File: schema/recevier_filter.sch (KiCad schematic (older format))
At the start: 14 parts, among them U7 LM358, U8 LM393

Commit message: Reception: schmidt trigger
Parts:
- removed R19: 100kΩ, symbol R
- removed R20: 10kΩ, symbol R
- added R? (x2): 4.7kΩ, symbol R
- added R?: 10kΩ, symbol R
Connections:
- net +5V: now also R?.1
- net GND: now also R?.2
- net SIGNAL: now also R?.1
- net at R18.1, U?.1: now also U8.2 (_); no longer U8.3 (+)
- new net: R?.1, R?.2, R?.2, U8.3 (+)
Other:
- note added: "Schmidt trigger"
- note removed: "Comparator"
- moved on the sheet: C?, R21, U8A
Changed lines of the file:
@@
 Comment4 ""
 $EndDescr
-Text HLabel 9700 3650 2    60   Output ~ 0
+Text HLabel 9700 3450 2    60   Output ~ 0
 SIGNAL
 $Comp
@@
 L LM393 U8
 U 1 1 5924C9D9
-P 8400 3650
-F 0 "U8" H 8550 3800 50  0000 C CNN
-F 1 "LM393" H 8650 3500 50  0000 C CNN
-F 2 "" H 8400 3650 50  0000 C CNN
-F 3 "" H 8400 3650 50  0000 C CNN
-	1    8400 3650
-	1    0    0    -1
-$EndComp
-$Comp
-L R R19
-U 1 1 5924CC18
-P 7600 3750
-F 0 "R19" V 7680 3750 50  0000 C CNN
-F 1 "100kΩ" V 7500 3750 50  0000 C CNN
-F 2 "" V 7530 3750 50  0000 C CNN
-F 3 "" H 7600 3750 50  0000 C CNN
-	1    7600 3750
-	0    1    1    0
-$EndComp
-$Comp
-L R R20
-U 1 1 5924CC6A
-P 7900 4050
-F 0 "R20" V 7980 4050 50  0000 C CNN
-F 1 "10kΩ" V 7800 4050 50  0000 C CNN
-F 2 "" V 7830 4050 50  0000 C CNN
-F 3 "" H 7900 4050 50  0000 C CNN
-	1    7900 4050
+P 8400 3450
+F 0 "U8" H 8550 3600 50  0000 C CNN
+F 1 "LM393" H 8650 3300 50  0000 C CNN
+F 2 "" H 8400 3450 50  0000 C CNN
+F 3 "" H 8400 3450 50  0000 C CNN
+	1    8400 3450
 	1    0    0    -1
 $EndComp
@@
 L GND #PWR23
 U 1 1 5924CCA3
-P 7900 4200
-F 0 "#PWR23" H 7900 3950 50  0001 C CNN
-F 1 "GND" H 7900 4050 50  0000 C CNN
-F 2 "" H 7900 4200 50  0000 C CNN
-F 3 "" H 7900 4200 50  0000 C CNN
-	1    7900 4200
+P 7600 4250
+F 0 "#PWR23" H 7600 4000 50  0001 C CNN
+F 1 "GND" H 7600 4100 50  0000 C CNN
+F 2 "" H 7600 4250 50  0000 C CNN
+F 3 "" H 7600 4250 50  0000 C CNN
+	1    7600 4250
 	1    0    0    -1
 $EndComp
@@
 L GND #PWR25
 U 1 1 5924CE19
-P 8300 3950
-F 0 "#PWR25" H 8300 3700 50  0001 C CNN
-F 1 "GND" H 8300 3800 50  0000 C CNN
-F 2 "" H 8300 3950 50  0000 C CNN
-F 3 "" H 8300 3950 50  0000 C CNN
-	1    8300 3950
+P 8300 4000
+F 0 "#PWR25" H 8300 3750 50  0001 C CNN
+F 1 "GND" H 8300 3850 50  0000 C CNN
+F 2 "" H 8300 4000 50  0000 C CNN
+F 3 "" H 8300 4000 50  0000 C CNN
+	1    8300 4000
 	1    0    0    -1
 $EndComp
@@
 L +5V #PWR24
 U 1 1 5924CE97
-P 8300 2950
-F 0 "#PWR24" H 8300 2800 50  0001 C CNN
-F 1 "+5V" H 8300 3090 50  0000 C CNN
-F 2 "" H 8300 2950 50  0000 C CNN
-F 3 "" H 8300 2950 50  0000 C CNN
-	1    8300 2950
+P 8300 2650
+F 0 "#PWR24" H 8300 2500 50  0001 C CNN
+F 1 "+5V" H 8300 2790 50  0000 C CNN
+F 2 "" H 8300 2650 50  0000 C CNN
+F 3 "" H 8300 2650 50  0000 C CNN
+	1    8300 2650
 	1    0    0    -1
 $EndComp
@@
 L +5V #PWR22
 U 1 1 5924CFDF
-P 7350 3750
-F 0 "#PWR22" H 7350 3600 50  0001 C CNN
-F 1 "+5V" H 7350 3890 50  0000 C CNN
-F 2 "" H 7350 3750 50  0000 C CNN
-F 3 "" H 7350 3750 50  0000 C CNN
-	1    7350 3750
-	1    0    0    -1
-$EndComp
-Wire Wire Line
-	7350 3750 7450 3750
-Wire Wire Line
-	7750 3750 8100 3750
-Wire Wire Line
-	7900 3900 7900 3750
-Connection ~ 7900 3750
-Wire Wire Line
-	8700 3650 9700 3650
+P 7600 2750
+F 0 "#PWR22" H 7600 2600 50  0001 C CNN
+F 1 "+5V" H 7600 2890 50  0000 C CNN
+F 2 "" H 7600 2750 50  0000 C CNN
+F 3 "" H 7600 2750 50  0000 C CNN
+	1    7600 2750
+	1    0    0    -1
+$EndComp
 Wire Notes Line
 	7250 2400 7250 4650
@@
 	9150 2400 7250 2400
 Text Notes 7350 4600 0    100  ~ 0
-Comparator
+Schmidt trigger
 $Comp
 L R R21
 U 1 1 5924DDAD
-P 8900 3400
-F 0 "R21" V 8980 3400 50  0000 C CNN
-F 1 "10kΩ" V 8800 3400 50  0000 C CNN
-F 2 "" V 8830 3400 50  0000 C CNN
-F 3 "" H 8900 3400 50  0000 C CNN
-	1    8900 3400
-	1    0    0    -1
-$EndComp
-Wire Wire Line
-	8900 3550 8900 3650
-Connection ~ 8900 3650
+P 8900 3150
+F 0 "R21" V 8980 3150 50  0000 C CNN
+F 1 "10kΩ" V 8800 3150 50  0000 C CNN
+F 2 "" V 8830 3150 50  0000 C CNN
+F 3 "" H 8900 3150 50  0000 C CNN
+	1    8900 3150
+	1    0    0    -1
+$EndComp
 $Comp
 L +5V #PWR26
 U 1 1 5924DE3C
-P 8900 3250
-F 0 "#PWR26" H 8900 3100 50  0001 C CNN
-F 1 "+5V" H 8900 3390 50  0000 C CNN
-F 2 "" H 8900 3250 50  0000 C CNN
-F 3 "" H 8900 3250 50  0000 C CNN
-	1    8900 3250
+P 8900 2950
+F 0 "#PWR26" H 8900 2800 50  0001 C CNN
+F 1 "+5V" H 8900 3090 50  0000 C CNN
+F 2 "" H 8900 2950 50  0000 C CNN
+F 3 "" H 8900 2950 50  0000 C CNN
+	1    8900 2950
 	1    0    0    -1
 $EndComp
@@
 L C C?
 U 1 1 59253FAB
-P 7950 3100
-F 0 "C?" H 7975 3200 50  0000 L CNN
-F 1 "100nF" H 7975 3000 50  0000 L CNN
-F 2 "" H 7988 2950 50  0000 C CNN
-F 3 "" H 7950 3100 50  0000 C CNN
-	1    7950 3100
+P 7950 2800
+F 0 "C?" H 7975 2900 50  0000 L CNN
+F 1 "100nF" H 7975 2700 50  0000 L CNN
+F 2 "" H 7988 2650 50  0000 C CNN
+F 3 "" H 7950 2800 50  0000 C CNN
+	1    7950 2800
 	1    0    0    -1
 $EndComp
@@
 L GND #PWR?
 U 1 1 5925407F
-P 7950 3250
-F 0 "#PWR?" H 7950 3000 50  0001 C CNN
-F 1 "GND" H 7950 3100 50  0000 C CNN
-F 2 "" H 7950 3250 50  0000 C CNN
-F 3 "" H 7950 3250 50  0000 C CNN
-	1    7950 3250
-	1    0    0    -1
-$EndComp
-Wire Wire Line
-	7950 2950 8300 2950
-Wire Wire Line
-	8300 2950 8300 3350
+P 7950 2950
+F 0 "#PWR?" H 7950 2700 50  0001 C CNN
+F 1 "GND" H 7950 2800 50  0000 C CNN
+F 2 "" H 7950 2950 50  0000 C CNN
+F 3 "" H 7950 2950 50  0000 C CNN
+	1    7950 2950
+	1    0    0    -1
+$EndComp
+Wire Wire Line
+	7950 2650 8300 2650
+$Comp
+L R R?
+U 1 1 592F2986
+P 7600 3050
+F 0 "R?" V 7680 3050 50  0000 C CNN
+F 1 "4.7kΩ" V 7500 3050 50  0000 C CNN
+F 2 "" V 7530 3050 50  0000 C CNN
+F 3 "" H 7600 3050 50  0000 C CNN
+	1    7600 3050
+	1    0    0    -1
+$EndComp
+$Comp
+L R R?
+U 1 1 592F2B41
+P 7600 4000
+F 0 "R?" V 7680 4000 50  0000 C CNN
+F 1 "10kΩ" V 7500 4000 50  0000 C CNN
+F 2 "" V 7530 4000 50  0000 C CNN
+F 3 "" H 7600 4000 50  0000 C CNN
+	1    7600 4000
+	1    0    0    -1
+$EndComp
+Wire Wire Line
+	8700 3450 9700 3450
+Wire Wire Line
+	8900 3300 8900 3800
+Connection ~ 8900 3450
+Wire Wire Line
+	7600 2750 7600 2900
+Wire Wire Line
+	7600 3200 7600 3850
+Wire Wire Line
+	7600 3350 8100 3350
+Connection ~ 7600 3350
+Wire Wire Line
+	7600 4150 7600 4250
+Connection ~ 7600 3800
+Wire Wire Line
+	8300 3750 8300 4000
+$Comp
+L R R?
+U 1 1 592F300B
+P 7950 3800
+F 0 "R?" V 8030 3800 50  0000 C CNN
+F 1 "4.7kΩ" V 7850 3800 50  0000 C CNN
+F 2 "" V 7880 3800 50  0000 C CNN
+F 3 "" H 7950 3800 50  0000 C CNN
+	1    7950 3800
+	0    1    1    0
+$EndComp
+Wire Wire Line
+	7600 3800 7800 3800
+Wire Wire Line
+	8900 3800 8100 3800
+Wire Wire Line
+	8900 2950 8900 3000
+Wire Wire Line
+	8300 2650 8300 3150
 $EndSCHEMATC

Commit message: reannotate schema
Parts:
- gave numbers to parts that had none: 5
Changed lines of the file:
@@
 $Descr A4 11693 8268
 encoding utf-8
-Sheet 4 6
+Sheet 3 6
 Title ""
 Date ""
@@
 $EndComp
 $Comp
-L GND #PWR17
+L GND #PWR9
 U 1 1 591066FE
 P 2900 3950
-F 0 "#PWR17" H 2900 3700 50  0001 C CNN
+F 0 "#PWR9" H 2900 3700 50  0001 C CNN
 F 1 "GND" H 2900 3800 50  0000 C CNN
 F 2 "" H 2900 3950 50  0000 C CNN
@@
 $EndComp
 $Comp
-L GND #PWR18
+L GND #PWR10
 U 1 1 59106802
 P 4750 3950
-F 0 "#PWR18" H 4750 3700 50  0001 C CNN
+F 0 "#PWR10" H 4750 3700 50  0001 C CNN
 F 1 "GND" H 4750 3800 50  0000 C CNN
 F 2 "" H 4750 3950 50  0000 C CNN
@@
 Connection ~ 4750 3650
 $Comp
-L +5V #PWR16
+L +5V #PWR8
 U 1 1 5910696F
 P 2900 3350
-F 0 "#PWR16" H 2900 3200 50  0001 C CNN
+F 0 "#PWR8" H 2900 3200 50  0001 C CNN
 F 1 "+5V" H 2900 3490 50  0000 C CNN
 F 2 "" H 2900 3350 50  0000 C CNN
@@
 Connection ~ 3450 3650
 $Comp
-L GND #PWR15
+L GND #PWR7
 U 1 1 59109B08
 P 2600 3550
-F 0 "#PWR15" H 2600 3300 50  0001 C CNN
+F 0 "#PWR7" H 2600 3300 50  0001 C CNN
 F 1 "GND" H 2600 3400 50  0000 C CNN
 F 2 "" H 2600 3550 50  0000 C CNN
@@
 Connection ~ 6250 3550
 $Comp
-L GND #PWR19
+L GND #PWR11
 U 1 1 5910AC6D
 P 5000 4200
-F 0 "#PWR19" H 5000 3950 50  0001 C CNN
+F 0 "#PWR11" H 5000 3950 50  0001 C CNN
 F 1 "GND" H 5000 4050 50  0000 C CNN
 F 2 "" H 5000 4200 50  0000 C CNN
@@
 	5000 4200 5100 4200
 $Comp
-L +5V #PWR20
+L +5V #PWR12
 U 1 1 5910ADF1
 P 5800 3250
-F 0 "#PWR20" H 5800 3100 50  0001 C CNN
+F 0 "#PWR12" H 5800 3100 50  0001 C CNN
 F 1 "+5V" H 5800 3390 50  0000 C CNN
 F 2 "" H 5800 3250 50  0000 C CNN
@@
 $EndComp
 $Comp
-L GND #PWR21
+L GND #PWR13
 U 1 1 5910B09A
 P 5800 3850
-F 0 "#PWR21" H 5800 3600 50  0001 C CNN
+F 0 "#PWR13" H 5800 3600 50  0001 C CNN
 F 1 "GND" H 5800 3700 50  0000 C CNN
 F 2 "" H 5800 3850 50  0000 C CNN
@@
 Amplifier & highpass
 $Comp
-L GND #PWR14
+L GND #PWR6
 U 1 1 59131F36
 P 1250 3950
-F 0 "#PWR14" H 1250 3700 50  0001 C CNN
+F 0 "#PWR6" H 1250 3700 50  0001 C CNN
 F 1 "GND" H 1250 3800 50  0000 C CNN
 F 2 "" H 1250 3950 50  0000 C CNN
@@
 $EndComp
 $Comp
-L GND #PWR23
+L GND #PWR15
 U 1 1 5924CCA3
 P 7600 4250
-F 0 "#PWR23" H 7600 4000 50  0001 C CNN
+F 0 "#PWR15" H 7600 4000 50  0001 C CNN
 F 1 "GND" H 7600 4100 50  0000 C CNN
 F 2 "" H 7600 4250 50  0000 C CNN
@@
 $EndComp
 $Comp
-L GND #PWR25
+L GND #PWR18
 U 1 1 5924CE19
 P 8300 4000
-F 0 "#PWR25" H 8300 3750 50  0001 C CNN
+F 0 "#PWR18" H 8300 3750 50  0001 C CNN
 F 1 "GND" H 8300 3850 50  0000 C CNN
 F 2 "" H 8300 4000 50  0000 C CNN
@@
 $EndComp
 $Comp
-L +5V #PWR24
+L +5V #PWR17
 U 1 1 5924CE97
 P 8300 2650
-F 0 "#PWR24" H 8300 2500 50  0001 C CNN
+F 0 "#PWR17" H 8300 2500 50  0001 C CNN
 F 1 "+5V" H 8300 2790 50  0000 C CNN
 F 2 "" H 8300 2650 50  0000 C CNN
@@
 $EndComp
 $Comp
-L +5V #PWR22
+L +5V #PWR14
 U 1 1 5924CFDF
 P 7600 2750
-F 0 "#PWR22" H 7600 2600 50  0001 C CNN
+F 0 "#PWR14" H 7600 2600 50  0001 C CNN
 F 1 "+5V" H 7600 2890 50  0000 C CNN
 F 2 "" H 7600 2750 50  0000 C CNN
@@
 $EndComp
 $Comp
-L +5V #PWR26
+L +5V #PWR19
 U 1 1 5924DE3C
 P 8900 2950
-F 0 "#PWR26" H 8900 2800 50  0001 C CNN
+F 0 "#PWR19" H 8900 2800 50  0001 C CNN
 F 1 "+5V" H 8900 3090 50  0000 C CNN
 F 2 "" H 8900 2950 50  0000 C CNN
@@
 $EndComp
 $Comp
-L LM358 U?
+L LM358 U7
 U 1 1 5913218F
 P 5900 3550
-F 0 "U?" H 5900 3750 50  0000 L CNN
+F 0 "U7" H 5900 3750 50  0000 L CNN
 F 1 "LM358" H 5900 3350 50  0000 L CNN
 F 2 "" H 5900 3550 50  0000 C CNN
@@
 	5150 3450 5150 3650
 $Comp
-L C C?
+L C C5
 U 1 1 59253FAB
 P 7950 2800
-F 0 "C?" H 7975 2900 50  0000 L CNN
+F 0 "C5" H 7975 2900 50  0000 L CNN
 F 1 "100nF" H 7975 2700 50  0000 L CNN
 F 2 "" H 7988 2650 50  0000 C CNN
@@
 $EndComp
 $Comp
-L GND #PWR?
+L GND #PWR16
 U 1 1 5925407F
 P 7950 2950
-F 0 "#PWR?" H 7950 2700 50  0001 C CNN
+F 0 "#PWR16" H 7950 2700 50  0001 C CNN
 F 1 "GND" H 7950 2800 50  0000 C CNN
 F 2 "" H 7950 2950 50  0000 C CNN
@@
 	7950 2650 8300 2650
 $Comp
-L R R?
+L R R9
 U 1 1 592F2986
 P 7600 3050
-F 0 "R?" V 7680 3050 50  0000 C CNN
+F 0 "R9" V 7680 3050 50  0000 C CNN
 F 1 "4.7kΩ" V 7500 3050 50  0000 C CNN
 F 2 "" V 7530 3050 50  0000 C CNN
@@
 $EndComp
 $Comp
-L R R?
+L R R10
 U 1 1 592F2B41
 P 7600 4000
-F 0 "R?" V 7680 4000 50  0000 C CNN
+F 0 "R10" V 7680 4000 50  0000 C CNN
 F 1 "10kΩ" V 7500 4000 50  0000 C CNN
 F 2 "" V 7530 4000 50  0000 C CNN
@@
 	8300 3750 8300 4000
 $Comp
-L R R?
+L R R11
 U 1 1 592F300B
 P 7950 3800
-F 0 "R?" V 8030 3800 50  0000 C CNN
+F 0 "R11" V 8030 3800 50  0000 C CNN
 F 1 "4.7kΩ" V 7850 3800 50  0000 C CNN
 F 2 "" V 7880 3800 50  0000 C CNN

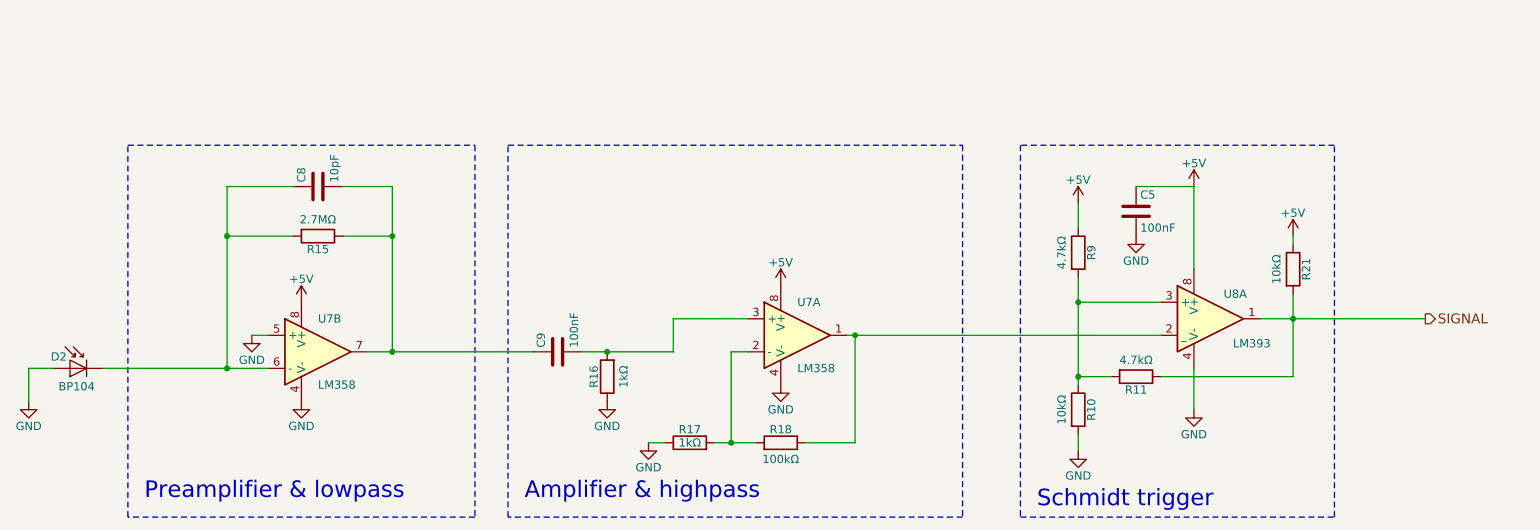
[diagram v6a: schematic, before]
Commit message: Schematic done
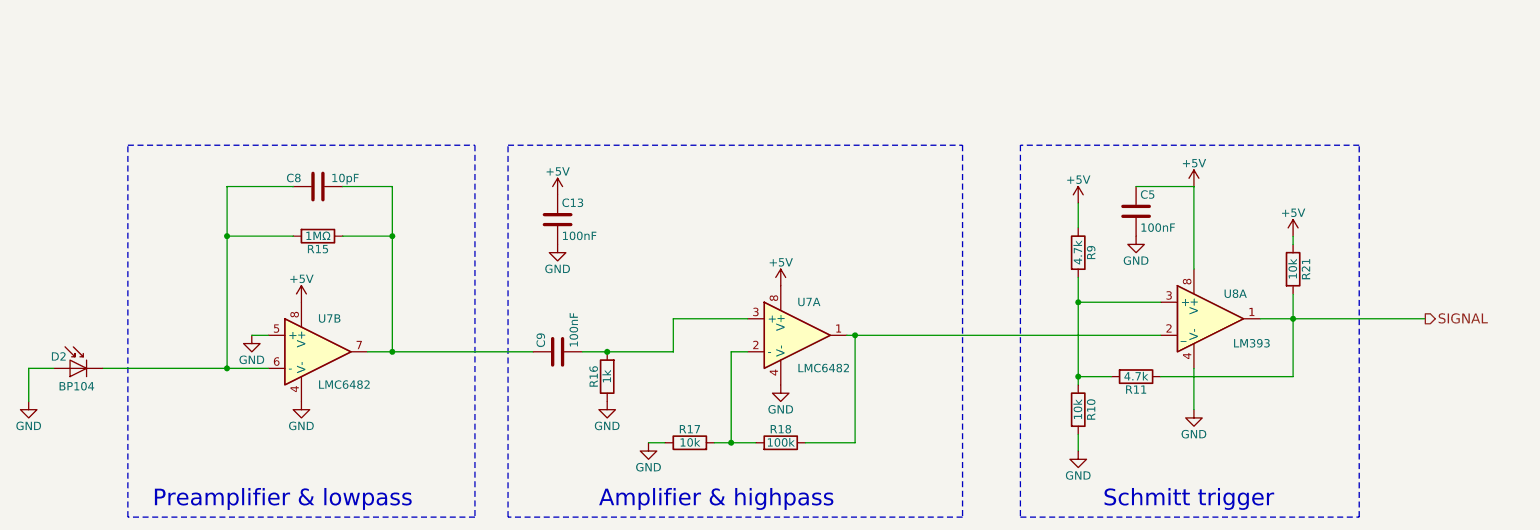
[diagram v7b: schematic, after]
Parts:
- added C13: 100nF, symbol C
- R10, R21: value 10kΩ -> 10k
- R11, R9: value 4.7kΩ -> 4.7k
- R15: value 2.7MΩ -> 1MΩ
- R16: value 1kΩ -> 1k
- R17: value 1kΩ -> 10k
- R18: value 100kΩ -> 100k
- U7: value LM358 -> LMC6482
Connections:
- net +5V: now also C13.1
- net GND: now also C13.2
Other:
- note added: "Schmitt trigger"
- note removed: "Schmidt trigger"
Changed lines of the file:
@@
 encoding utf-8
 Sheet 3 6
-Title ""
+Title "Recevier / Filter"
 Date ""
 Rev ""
@@
 P 4750 3800
 F 0 "R16" V 4830 3800 50  0000 C CNN
-F 1 "1kΩ" V 4650 3800 50  0000 C CNN
+F 1 "1k" V 4750 3800 50  0000 C CNN
 F 2 "" V 4680 3800 50  0000 C CNN
 F 3 "" H 4750 3800 50  0000 C CNN
@@
 $EndComp
 $Comp
-L GND #PWR10
+L GND #PWR12
 U 1 1 59106802
 P 4750 3950
-F 0 "#PWR10" H 4750 3700 50  0001 C CNN
+F 0 "#PWR12" H 4750 3700 50  0001 C CNN
 F 1 "GND" H 4750 3800 50  0000 C CNN
 F 2 "" H 4750 3950 50  0000 C CNN
@@
 $EndComp
 Wire Wire Line
-	3300 3650 4300 3650
-Wire Wire Line
-	4600 3650 5150 3650
+	3300 3650 3450 3650
+Wire Wire Line
+	3450 3650 4300 3650
+Wire Wire Line
+	4600 3650 4750 3650
+Wire Wire Line
+	4750 3650 5150 3650
 Connection ~ 4750 3650
 $Comp
@@
 $EndComp
 Wire Wire Line
-	1700 3750 2700 3750
+	1700 3750 2450 3750
+Wire Wire Line
+	2450 3750 2700 3750
 Wire Wire Line
 	1250 3750 1250 3950
@@
 P 3000 2950
 F 0 "R15" V 3080 2950 50  0000 C CNN
-F 1 "2.7MΩ" V 2900 2950 50  0000 C CNN
+F 1 "1MΩ" V 3000 2950 50  0000 C CNN
 F 2 "" V 2930 2950 50  0000 C CNN
 F 3 "" H 3000 2950 50  0000 C CNN
@@
 P 5800 4200
 F 0 "R18" V 5880 4200 50  0000 C CNN
-F 1 "100kΩ" V 5700 4200 50  0000 C CNN
+F 1 "100k" V 5800 4200 50  0000 C CNN
 F 2 "" V 5730 4200 50  0000 C CNN
 F 3 "" H 5800 4200 50  0000 C CNN
@@
 P 5250 4200
 F 0 "R17" V 5330 4200 50  0000 C CNN
-F 1 "1kΩ" V 5250 4200 50  0000 C CNN
+F 1 "10k" V 5250 4200 50  0000 C CNN
 F 2 "" V 5180 4200 50  0000 C CNN
 F 3 "" H 5250 4200 50  0000 C CNN
@@
 $EndComp
 Wire Wire Line
-	6200 3550 8100 3550
-Wire Wire Line
-	5400 4200 5650 4200
+	6200 3550 6250 3550
+Wire Wire Line
+	6250 3550 8100 3550
+Wire Wire Line
+	5400 4200 5500 4200
+Wire Wire Line
+	5500 4200 5650 4200
 Connection ~ 5500 4200
 Wire Wire Line
@@
 Connection ~ 6250 3550
 $Comp
-L GND #PWR11
+L GND #PWR13
 U 1 1 5910AC6D
 P 5000 4200
-F 0 "#PWR11" H 5000 3950 50  0001 C CNN
+F 0 "#PWR13" H 5000 3950 50  0001 C CNN
 F 1 "GND" H 5000 4050 50  0000 C CNN
 F 2 "" H 5000 4200 50  0000 C CNN
@@
 	5000 4200 5100 4200
 $Comp
-L +5V #PWR12
+L +5V #PWR14
 U 1 1 5910ADF1
 P 5800 3250
-F 0 "#PWR12" H 5800 3100 50  0001 C CNN
+F 0 "#PWR14" H 5800 3100 50  0001 C CNN
 F 1 "+5V" H 5800 3390 50  0000 C CNN
 F 2 "" H 5800 3250 50  0000 C CNN
@@
 $EndComp
 $Comp
-L GND #PWR13
+L GND #PWR15
 U 1 1 5910B09A
 P 5800 3850
-F 0 "#PWR13" H 5800 3600 50  0001 C CNN
+F 0 "#PWR15" H 5800 3600 50  0001 C CNN
 F 1 "GND" H 5800 3700 50  0000 C CNN
 F 2 "" H 5800 3850 50  0000 C CNN
@@
 Wire Wire Line
 	1400 3750 1250 3750
-Text Notes 1950 4550 0    100  ~ 0
+Text Notes 2000 4600 0    100  ~ 0
 Preamplifier & lowpass
-Text Notes 4250 4550 0    100  ~ 0
+Text Notes 4700 4600 0    100  ~ 0
 Amplifier & highpass
 $Comp
@@
 P 3000 3650
 F 0 "U7" H 3000 3850 50  0000 L CNN
-F 1 "LM358" H 3000 3450 50  0000 L CNN
+F 1 "LMC6482" H 3000 3450 50  0000 L CNN
 F 2 "" H 3000 3650 50  0000 C CNN
 F 3 "" H 3000 3650 50  0000 C CNN
@@
 Connection ~ 2450 3750
 Wire Wire Line
-	2450 2650 2450 3750
-Wire Wire Line
-	3450 2650 3450 3650
+	2450 2650 2450 2950
+Wire Wire Line
+	2450 2950 2450 3750
+Wire Wire Line
+	3450 2650 3450 2950
+Wire Wire Line
+	3450 2950 3450 3650
 $Comp
 L C C8
 U 1 1 5921D2F3
 P 3000 2650
-F 0 "C8" H 3025 2750 50  0000 L CNN
-F 1 "10pF" H 3025 2550 50  0000 L CNN
+F 0 "C8" V 3050 2750 50  0000 L CNN
+F 1 "10pF" V 3050 2400 50  0000 L CNN
 F 2 "" H 3038 2500 50  0000 C CNN
 F 3 "" H 3000 2650 50  0000 C CNN
@@
 $EndComp
 $Comp
-L GND #PWR15
+L GND #PWR17
 U 1 1 5924CCA3
 P 7600 4250
-F 0 "#PWR15" H 7600 4000 50  0001 C CNN
+F 0 "#PWR17" H 7600 4000 50  0001 C CNN
 F 1 "GND" H 7600 4100 50  0000 C CNN
 F 2 "" H 7600 4250 50  0000 C CNN
@@
 $EndComp
 $Comp
-L GND #PWR18
+L GND #PWR20
 U 1 1 5924CE19
 P 8300 4000
-F 0 "#PWR18" H 8300 3750 50  0001 C CNN
+F 0 "#PWR20" H 8300 3750 50  0001 C CNN
 F 1 "GND" H 8300 3850 50  0000 C CNN
 F 2 "" H 8300 4000 50  0000 C CNN
@@
 $EndComp
 $Comp
-L +5V #PWR17
+L +5V #PWR19
 U 1 1 5924CE97
 P 8300 2650
-F 0 "#PWR17" H 8300 2500 50  0001 C CNN
+F 0 "#PWR19" H 8300 2500 50  0001 C CNN
 F 1 "+5V" H 8300 2790 50  0000 C CNN
 F 2 "" H 8300 2650 50  0000 C CNN
@@
 $EndComp
 $Comp
-L +5V #PWR14
+L +5V #PWR16
 U 1 1 5924CFDF
 P 7600 2750
-F 0 "#PWR14" H 7600 2600 50  0001 C CNN
+F 0 "#PWR16" H 7600 2600 50  0001 C CNN
 F 1 "+5V" H 7600 2890 50  0000 C CNN
 F 2 "" H 7600 2750 50  0000 C CNN
@@
 	7250 2400 7250 4650
 Wire Notes Line
-	7250 4650 9150 4650
-Wire Notes Line
-	9150 4650 9150 2400
-Wire Notes Line
-	9150 2400 7250 2400
-Text Notes 7350 4600 0    100  ~ 0
-Schmidt trigger
+	7250 4650 9300 4650
+Wire Notes Line
+	9300 4650 9300 2400
+Wire Notes Line
+	9300 2400 7250 2400
+Text Notes 7750 4600 0    100  ~ 0
+Schmitt trigger
 $Comp
 L R R21
@@
 P 8900 3150
 F 0 "R21" V 8980 3150 50  0000 C CNN
-F 1 "10kΩ" V 8800 3150 50  0000 C CNN
+F 1 "10k" V 8900 3150 50  0000 C CNN
 F 2 "" V 8830 3150 50  0000 C CNN
 F 3 "" H 8900 3150 50  0000 C CNN
@@
 $EndComp
 $Comp
-L +5V #PWR19
+L +5V #PWR21
 U 1 1 5924DE3C
 P 8900 2950
-F 0 "#PWR19" H 8900 2800 50  0001 C CNN
+F 0 "#PWR21" H 8900 2800 50  0001 C CNN
 F 1 "+5V" H 8900 3090 50  0000 C CNN
 F 2 "" H 8900 2950 50  0000 C CNN
@@
 P 5900 3550
 F 0 "U7" H 5900 3750 50  0000 L CNN
-F 1 "LM358" H 5900 3350 50  0000 L CNN
+F 1 "LMC6482" H 5900 3350 50  0000 L CNN
 F 2 "" H 5900 3550 50  0000 C CNN
 F 3 "" H 5900 3550 50  0000 C CNN
@@
 $EndComp
 $Comp
-L GND #PWR16
+L GND #PWR18
 U 1 1 5925407F
 P 7950 2950
-F 0 "#PWR16" H 7950 2700 50  0001 C CNN
+F 0 "#PWR18" H 7950 2700 50  0001 C CNN
 F 1 "GND" H 7950 2800 50  0000 C CNN
 F 2 "" H 7950 2950 50  0000 C CNN
@@
 P 7600 3050
 F 0 "R9" V 7680 3050 50  0000 C CNN
-F 1 "4.7kΩ" V 7500 3050 50  0000 C CNN
+F 1 "4.7k" V 7600 3050 50  0000 C CNN
 F 2 "" V 7530 3050 50  0000 C CNN
 F 3 "" H 7600 3050 50  0000 C CNN
@@
 P 7600 4000
 F 0 "R10" V 7680 4000 50  0000 C CNN
-F 1 "10kΩ" V 7500 4000 50  0000 C CNN
+F 1 "10k" V 7600 4000 50  0000 C CNN
 F 2 "" V 7530 4000 50  0000 C CNN
 F 3 "" H 7600 4000 50  0000 C CNN
@@
 $EndComp
 Wire Wire Line
-	8700 3450 9700 3450
-Wire Wire Line
-	8900 3300 8900 3800
+	8700 3450 8900 3450
+Wire Wire Line
+	8900 3450 9700 3450
+Wire Wire Line
+	8900 3300 8900 3450
+Wire Wire Line
+	8900 3450 8900 3800
 Connection ~ 8900 3450
 Wire Wire Line
 	7600 2750 7600 2900
 Wire Wire Line
-	7600 3200 7600 3850
+	7600 3200 7600 3350
+Wire Wire Line
+	7600 3350 7600 3800
+Wire Wire Line
+	7600 3800 7600 3850
 Wire Wire Line
 	7600 3350 8100 3350
@@
 P 7950 3800
 F 0 "R11" V 8030 3800 50  0000 C CNN
-F 1 "4.7kΩ" V 7850 3800 50  0000 C CNN
+F 1 "4.7k" V 7950 3800 50  0000 C CNN
 F 2 "" V 7880 3800 50  0000 C CNN
 F 3 "" H 7950 3800 50  0000 C CNN
@@
 Wire Wire Line
 	8300 2650 8300 3150
+$Comp
+L C C13
+U 1 1 593EB278
+P 4450 2850
+F 0 "C13" H 4475 2950 50  0000 L CNN
+F 1 "100nF" H 4475 2750 50  0000 L CNN
+F 2 "" H 4488 2700 50  0000 C CNN
+F 3 "" H 4450 2850 50  0000 C CNN
+	1    4450 2850
+	1    0    0    -1
+$EndComp
+$Comp
+L GND #PWR11
+U 1 1 593EB2BE
+P 4450 3000
+F 0 "#PWR11" H 4450 2750 50  0001 C CNN
+F 1 "GND" H 4450 2850 50  0000 C CNN
+F 2 "" H 4450 3000 50  0000 C CNN
+F 3 "" H 4450 3000 50  0000 C CNN
+	1    4450 3000
+	1    0    0    -1
+$EndComp
+$Comp
+L +5V #PWR10
+U 1 1 593EB309
+P 4450 2700
+F 0 "#PWR10" H 4450 2550 50  0001 C CNN
+F 1 "+5V" H 4450 2840 50  0000 C CNN
+F 2 "" H 4450 2700 50  0000 C CNN
+F 3 "" H 4450 2700 50  0000 C CNN
+	1    4450 2700
+	1    0    0    -1
+$EndComp
 $EndSCHEMATC
